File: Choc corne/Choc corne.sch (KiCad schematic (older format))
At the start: 43 parts, among them U1 ProMicro

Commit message: Started pcb
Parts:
- added J1: MJ-4PP-9, symbol kbd:MJ-4PP-9
- added OL1: OLED, symbol kbd:OLED
- added SW1: SW_PUSH, symbol kbd:SW_PUSH
- MX1, MX10, MX11, MX12, MX13, MX14, MX15, MX16, MX17, MX18, MX19, MX2, MX20, MX3, MX4, MX5, MX6, MX7, MX8, MX9: footprint Keebio-Parts:MX-Alps-Choc-1U-NoLED -> Keebio-Parts:Kailh-PG1350-1u-NoLED
- MX21: footprint Keebio-Parts:MX-Alps-Choc-1U-NoLED -> Keebio-Parts:Kailh-PG1350-1.5u
- U1: value ProMicro -> Elite-C; footprint Keebio-Parts:Elite-C-ZigZag -> Keebio-Parts:Elite-C
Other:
- moved on the sheet: U1
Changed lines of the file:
@@
 L promicro:ProMicro U1
 U 1 1 64503A13
-P 6050 3750
-F 0 "U1" H 6050 4787 60  0000 C CNN
-F 1 "ProMicro" H 6050 4681 60  0000 C CNN
-F 2 "Keebio-Parts:Elite-C-ZigZag" H 6150 2700 60  0001 C CNN
-F 3 "" H 6150 2700 60  0000 C CNN
-	1    6050 3750
+P 6100 3050
+F 0 "U1" H 6100 4087 60  0000 C CNN
+F 1 "Elite-C" H 6100 3981 60  0000 C CNN
+F 2 "Keebio-Parts:Elite-C" H 6200 2000 60  0001 C CNN
+F 3 "" H 6200 2000 60  0000 C CNN
+	1    6100 3050
 	1    0    0    -1
 $EndComp
@@
 F 0 "MX1" H 1583 2823 60  0000 C CNN
 F 1 "MX-NoLED" H 1583 2749 20  0000 C CNN
-F 2 "Keebio-Parts:MX-Alps-Choc-1U-NoLED" H 925 2575 60  0001 C CNN
+F 2 "Keebio-Parts:Kailh-PG1350-1u-NoLED" H 925 2575 60  0001 C CNN
 F 3 "" H 925 2575 60  0001 C CNN
 	1    1550 2600
@@
 F 0 "MX2" H 2183 2823 60  0000 C CNN
 F 1 "MX-NoLED" H 2183 2749 20  0000 C CNN
-F 2 "Keebio-Parts:MX-Alps-Choc-1U-NoLED" H 1525 2575 60  0001 C CNN
+F 2 "Keebio-Parts:Kailh-PG1350-1u-NoLED" H 1525 2575 60  0001 C CNN
 F 3 "" H 1525 2575 60  0001 C CNN
 	1    2150 2600
@@
 F 0 "MX3" H 2783 2823 60  0000 C CNN
 F 1 "MX-NoLED" H 2783 2749 20  0000 C CNN
-F 2 "Keebio-Parts:MX-Alps-Choc-1U-NoLED" H 2125 2575 60  0001 C CNN
+F 2 "Keebio-Parts:Kailh-PG1350-1u-NoLED" H 2125 2575 60  0001 C CNN
 F 3 "" H 2125 2575 60  0001 C CNN
 	1    2750 2600
@@
 F 0 "MX4" H 3383 2823 60  0000 C CNN
 F 1 "MX-NoLED" H 3383 2749 20  0000 C CNN
-F 2 "Keebio-Parts:MX-Alps-Choc-1U-NoLED" H 2725 2575 60  0001 C CNN
+F 2 "Keebio-Parts:Kailh-PG1350-1u-NoLED" H 2725 2575 60  0001 C CNN
 F 3 "" H 2725 2575 60  0001 C CNN
 	1    3350 2600
@@
 F 0 "MX5" H 3983 2823 60  0000 C CNN
 F 1 "MX-NoLED" H 3983 2749 20  0000 C CNN
-F 2 "Keebio-Parts:MX-Alps-Choc-1U-NoLED" H 3325 2575 60  0001 C CNN
+F 2 "Keebio-Parts:Kailh-PG1350-1u-NoLED" H 3325 2575 60  0001 C CNN
 F 3 "" H 3325 2575 60  0001 C CNN
 	1    3950 2600
@@
 F 0 "MX6" H 4583 2823 60  0000 C CNN
 F 1 "MX-NoLED" H 4583 2749 20  0000 C CNN
-F 2 "Keebio-Parts:MX-Alps-Choc-1U-NoLED" H 3925 2575 60  0001 C CNN
+F 2 "Keebio-Parts:Kailh-PG1350-1u-NoLED" H 3925 2575 60  0001 C CNN
 F 3 "" H 3925 2575 60  0001 C CNN
 	1    4550 2600
@@
 F 0 "MX7" H 1583 3573 60  0000 C CNN
 F 1 "MX-NoLED" H 1583 3499 20  0000 C CNN
-F 2 "Keebio-Parts:MX-Alps-Choc-1U-NoLED" H 925 3325 60  0001 C CNN
+F 2 "Keebio-Parts:Kailh-PG1350-1u-NoLED" H 925 3325 60  0001 C CNN
 F 3 "" H 925 3325 60  0001 C CNN
 	1    1550 3350
@@
 F 0 "MX8" H 2183 3573 60  0000 C CNN
 F 1 "MX-NoLED" H 2183 3499 20  0000 C CNN
-F 2 "Keebio-Parts:MX-Alps-Choc-1U-NoLED" H 1525 3325 60  0001 C CNN
+F 2 "Keebio-Parts:Kailh-PG1350-1u-NoLED" H 1525 3325 60  0001 C CNN
 F 3 "" H 1525 3325 60  0001 C CNN
 	1    2150 3350
@@
 F 0 "MX9" H 2783 3573 60  0000 C CNN
 F 1 "MX-NoLED" H 2783 3499 20  0000 C CNN
-F 2 "Keebio-Parts:MX-Alps-Choc-1U-NoLED" H 2125 3325 60  0001 C CNN
+F 2 "Keebio-Parts:Kailh-PG1350-1u-NoLED" H 2125 3325 60  0001 C CNN
 F 3 "" H 2125 3325 60  0001 C CNN
 	1    2750 3350
@@
 F 0 "MX10" H 3383 3573 60  0000 C CNN
 F 1 "MX-NoLED" H 3383 3499 20  0000 C CNN
-F 2 "Keebio-Parts:MX-Alps-Choc-1U-NoLED" H 2725 3325 60  0001 C CNN
+F 2 "Keebio-Parts:Kailh-PG1350-1u-NoLED" H 2725 3325 60  0001 C CNN
 F 3 "" H 2725 3325 60  0001 C CNN
 	1    3350 3350
@@
 F 0 "MX11" H 3983 3573 60  0000 C CNN
 F 1 "MX-NoLED" H 3983 3499 20  0000 C CNN
-F 2 "Keebio-Parts:MX-Alps-Choc-1U-NoLED" H 3325 3325 60  0001 C CNN
+F 2 "Keebio-Parts:Kailh-PG1350-1u-NoLED" H 3325 3325 60  0001 C CNN
 F 3 "" H 3325 3325 60  0001 C CNN
 	1    3950 3350
@@
 F 0 "MX12" H 4583 3573 60  0000 C CNN
 F 1 "MX-NoLED" H 4583 3499 20  0000 C CNN
-F 2 "Keebio-Parts:MX-Alps-Choc-1U-NoLED" H 3925 3325 60  0001 C CNN
+F 2 "Keebio-Parts:Kailh-PG1350-1u-NoLED" H 3925 3325 60  0001 C CNN
 F 3 "" H 3925 3325 60  0001 C CNN
 	1    4550 3350
@@
 F 0 "MX13" H 1583 4323 60  0000 C CNN
 F 1 "MX-NoLED" H 1583 4249 20  0000 C CNN
-F 2 "Keebio-Parts:MX-Alps-Choc-1U-NoLED" H 925 4075 60  0001 C CNN
+F 2 "Keebio-Parts:Kailh-PG1350-1u-NoLED" H 925 4075 60  0001 C CNN
 F 3 "" H 925 4075 60  0001 C CNN
 	1    1550 4100
@@
 F 0 "MX14" H 2183 4323 60  0000 C CNN
 F 1 "MX-NoLED" H 2183 4249 20  0000 C CNN
-F 2 "Keebio-Parts:MX-Alps-Choc-1U-NoLED" H 1525 4075 60  0001 C CNN
+F 2 "Keebio-Parts:Kailh-PG1350-1u-NoLED" H 1525 4075 60  0001 C CNN
 F 3 "" H 1525 4075 60  0001 C CNN
 	1    2150 4100
@@
 F 0 "MX15" H 2783 4323 60  0000 C CNN
 F 1 "MX-NoLED" H 2783 4249 20  0000 C CNN
-F 2 "Keebio-Parts:MX-Alps-Choc-1U-NoLED" H 2125 4075 60  0001 C CNN
+F 2 "Keebio-Parts:Kailh-PG1350-1u-NoLED" H 2125 4075 60  0001 C CNN
 F 3 "" H 2125 4075 60  0001 C CNN
 	1    2750 4100
@@
 F 0 "MX16" H 3383 4323 60  0000 C CNN
 F 1 "MX-NoLED" H 3383 4249 20  0000 C CNN
-F 2 "Keebio-Parts:MX-Alps-Choc-1U-NoLED" H 2725 4075 60  0001 C CNN
+F 2 "Keebio-Parts:Kailh-PG1350-1u-NoLED" H 2725 4075 60  0001 C CNN
 F 3 "" H 2725 4075 60  0001 C CNN
 	1    3350 4100
@@
 F 0 "MX17" H 3983 4323 60  0000 C CNN
 F 1 "MX-NoLED" H 3983 4249 20  0000 C CNN
-F 2 "Keebio-Parts:MX-Alps-Choc-1U-NoLED" H 3325 4075 60  0001 C CNN
+F 2 "Keebio-Parts:Kailh-PG1350-1u-NoLED" H 3325 4075 60  0001 C CNN
 F 3 "" H 3325 4075 60  0001 C CNN
 	1    3950 4100
@@
 F 0 "MX18" H 4583 4323 60  0000 C CNN
 F 1 "MX-NoLED" H 4583 4249 20  0000 C CNN
-F 2 "Keebio-Parts:MX-Alps-Choc-1U-NoLED" H 3925 4075 60  0001 C CNN
+F 2 "Keebio-Parts:Kailh-PG1350-1u-NoLED" H 3925 4075 60  0001 C CNN
 F 3 "" H 3925 4075 60  0001 C CNN
 	1    4550 4100
@@
 F 0 "MX19" H 3383 5073 60  0000 C CNN
 F 1 "MX-NoLED" H 3383 4999 20  0000 C CNN
-F 2 "Keebio-Parts:MX-Alps-Choc-1U-NoLED" H 2725 4825 60  0001 C CNN
+F 2 "Keebio-Parts:Kailh-PG1350-1u-NoLED" H 2725 4825 60  0001 C CNN
 F 3 "" H 2725 4825 60  0001 C CNN
 	1    3350 4850
@@
 F 0 "MX20" H 3983 5073 60  0000 C CNN
 F 1 "MX-NoLED" H 3983 4999 20  0000 C CNN
-F 2 "Keebio-Parts:MX-Alps-Choc-1U-NoLED" H 3325 4825 60  0001 C CNN
+F 2 "Keebio-Parts:Kailh-PG1350-1u-NoLED" H 3325 4825 60  0001 C CNN
 F 3 "" H 3325 4825 60  0001 C CNN
 	1    3950 4850
@@
 F 0 "MX21" H 4583 5073 60  0000 C CNN
 F 1 "MX-NoLED" H 4583 4999 20  0000 C CNN
-F 2 "Keebio-Parts:MX-Alps-Choc-1U-NoLED" H 3925 4825 60  0001 C CNN
+F 2 "Keebio-Parts:Kailh-PG1350-1.5u" H 3925 4825 60  0001 C CNN
 F 3 "" H 3925 4825 60  0001 C CNN
 	1    4550 4850
@@
 Text GLabel 2800 5300 0    50   Input ~ 0
 ROW3
+$Comp
+L kbd:MJ-4PP-9 J1
+U 1 1 64591E95
+P 6000 5650
+F 0 "J1" H 5820 5608 50  0000 R CNN
+F 1 "MJ-4PP-9" H 5820 5699 50  0000 R CNN
+F 2 "" H 6275 5825 50  0001 C CNN
+F 3 "~" H 6275 5825 50  0001 C CNN
+	1    6000 5650
+	-1   0    0    1
+$EndComp
+$Comp
+L kbd:OLED OL1
+U 1 1 645939B3
+P 6050 4150
+F 0 "OL1" V 6011 3822 51  0000 R CNN
+F 1 "OLED" V 5921 3822 47  0000 R CNN
+F 2 "" H 6050 4250 60  0001 C CNN
+F 3 "" H 6050 4250 60  0001 C CNN
+	1    6050 4150
+	0    -1   -1   0
+$EndComp
+$Comp
+L kbd:SW_PUSH SW1
+U 1 1 64598CCE
+P 6050 5300
+F 0 "SW1" H 6050 5555 50  0000 C CNN
+F 1 "SW_PUSH" H 6050 5464 50  0000 C CNN
+F 2 "" H 6050 5300 50  0000 C CNN
+F 3 "" H 6050 5300 50  0000 C CNN
+	1    6050 5300
+	1    0    0    -1
+$EndComp
 $EndSCHEMATC

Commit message: big update
whatever
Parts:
- added D22, D23, D24, D25, D26, D27, D28, D29, D30, D31, D32, D33, D34, D35, D36, D37, D38, D39, D40, D41, D42: CD4148W, Diode_SMD:D_0805_2012Metric, symbol Diode:CD4148W
- added J2: MJ-4PP-9, Keebio-Parts:TRRS-PJ-320A, symbol kbd:MJ-4PP-9
- added MX22, MX23, MX24, MX25, MX26, MX27, MX28, MX29, MX30, MX31, MX32, MX33, MX34, MX35, MX36, MX37, MX38, MX39, MX41, MX42: MX-NoLED, kbd:CherryMX_ChocV2_1u, symbol MX_Alps_Hybrid:MX-NoLED
- added MX40: MX-NoLED, kbd:CherryMX_ChocV2_1.5u, symbol MX_Alps_Hybrid:MX-NoLED
- added OL2: OLED, kbd:OLED_1side, symbol kbd:OLED
- added SW2: SW_PUSH, kbd:ResetSW_1side, symbol kbd:SW_PUSH
- added U2: Elite-C, Keebio-Parts:Elite-C, symbol promicro:ProMicro
- J1: footprint (none) -> Keebio-Parts:TRRS-PJ-320A
- MX1, MX10, MX11, MX12, MX13, MX14, MX15, MX16, MX17, MX18, MX19, MX2, MX20, MX3, MX4, MX5, MX6, MX7, MX8, MX9: footprint Keebio-Parts:Kailh-PG1350-1u-NoLED -> kbd:CherryMX_ChocV2_1u
- MX21: footprint Keebio-Parts:Kailh-PG1350-1.5u -> kbd:CherryMX_ChocV2_1.5u
- OL1: footprint (none) -> kbd:OLED_1side
- SW1: footprint (none) -> kbd:ResetSW_1side
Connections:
- net DATA: now reaches U1.2 (RX)
- net DATA: now also J1.B
- net VCC: now reaches U1.21 (VCC)
- net VCC: now also J1.D, OL1.3 (VCC)
- net RESET: now reaches U1.22 (RST)
- net RESET: now also SW1.1
- net GND: now reaches U1.23 (GND)
- net GND: now also J1.C, OL1.4 (GND), SW1.2, U1.3 (GND), U1.4 (GND)
- net SDA: now reaches U1.5 (SDA)
- net SDA: now also OL1.1 (SDA)
- net SCL: now reaches U1.6 (SCL)
- net SCL: now also OL1.2 (SCL)
- new net: D22.2 (A), MX22.2 (ROW)
- new net: D23.2 (A), MX23.2 (ROW)
- new net: D24.2 (A), MX24.2 (ROW)
- new net: D25.2 (A), MX25.2 (ROW)
- new net: D26.2 (A), MX26.2 (ROW)
- new net: D27.2 (A), MX27.2 (ROW)
- new net: D28.2 (A), MX28.2 (ROW)
- new net: D29.2 (A), MX29.2 (ROW)
- new net: D30.2 (A), MX30.2 (ROW)
- new net: D31.2 (A), MX31.2 (ROW)
- new net: D32.2 (A), MX32.2 (ROW)
- new net: D33.2 (A), MX33.2 (ROW)
- new net: D34.2 (A), MX34.2 (ROW)
- new net: D35.2 (A), MX35.2 (ROW)
- new net: D36.2 (A), MX36.2 (ROW)
- new net: D37.2 (A), MX37.2 (ROW)
- new net: D38.2 (A), MX38.2 (ROW)
- new net: D39.2 (A), MX39.2 (ROW)
- new net: D40.2 (A), MX40.2 (ROW)
- new net: D41.2 (A), MX41.2 (ROW)
- new net: D42.2 (A), MX42.2 (ROW)
- new net COL10: MX26.1 (COL), MX32.1 (COL), MX38.1 (COL)
- new net COL11: MX27.1 (COL), MX33.1 (COL), MX39.1 (COL)
- new net COL6: MX22.1 (COL), MX28.1 (COL), MX34.1 (COL), MX40.1 (COL)
- new net COL7: MX23.1 (COL), MX29.1 (COL), MX35.1 (COL), MX41.1 (COL)
- new net COL8: MX24.1 (COL), MX30.1 (COL), MX36.1 (COL), MX42.1 (COL)
- new net COL9: MX25.1 (COL), MX31.1 (COL), MX37.1 (COL)
- new net DATA_R: J2.B, U2.2 (RX)
- new net GNDA: J2.C, OL2.4 (GND), SW2.2, U2.23 (GND), U2.3 (GND), U2.4 (GND)
- new net RESET_R: SW2.1, U2.22 (RST)
- new net ROW4: D22.1 (K), D23.1 (K), D24.1 (K), D25.1 (K), D26.1 (K), D27.1 (K)
- new net ROW5: D28.1 (K), D29.1 (K), D30.1 (K), D31.1 (K), D32.1 (K), D33.1 (K)
- new net ROW6: D34.1 (K), D35.1 (K), D36.1 (K), D37.1 (K), D38.1 (K), D39.1 (K)
- new net ROW8: D40.1 (K), D41.1 (K), D42.1 (K)
- new net SCL_R: OL2.2 (SCL), U2.5 (SDA), U2.6 (SCL)
- new net SDA_R: OL2.1 (SDA)
- new net VDD: J2.D, OL2.3 (VCC)
- no-connect marks 0 -> 4
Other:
- moved on the sheet: D1, D10, D11, D12, D13, D14, D15, D16, D17, D18, D19, D2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

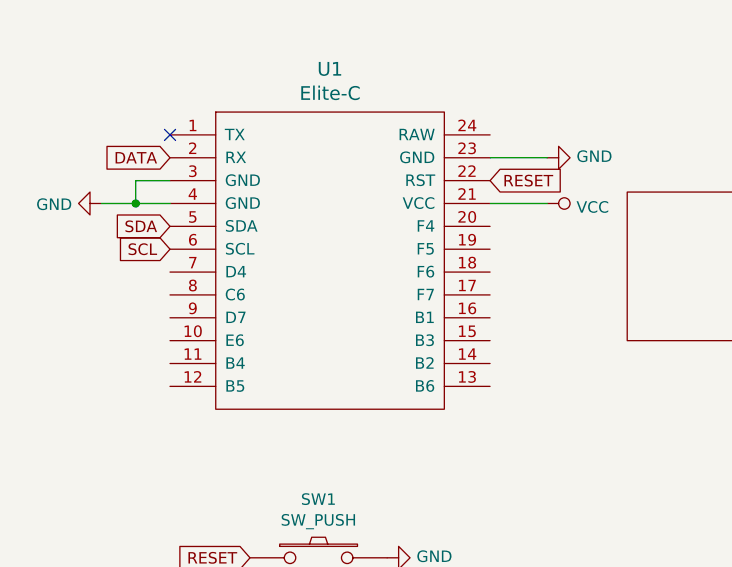
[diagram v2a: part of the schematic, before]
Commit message: Added partial pcb routing
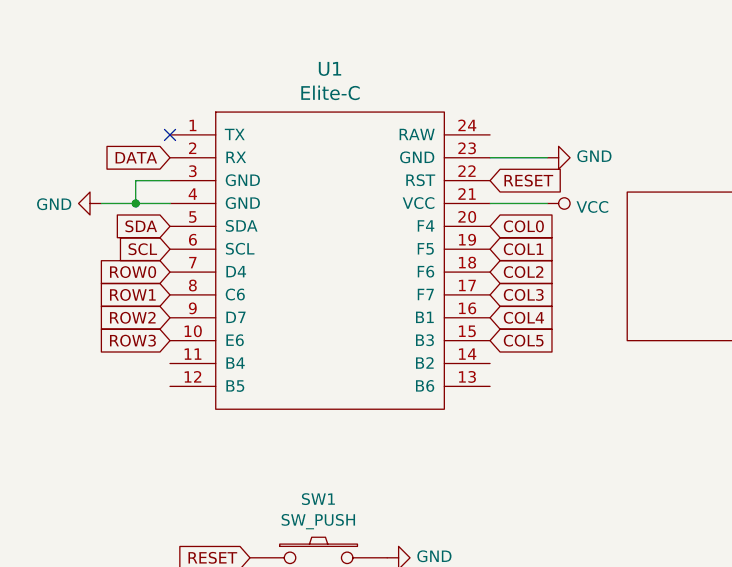
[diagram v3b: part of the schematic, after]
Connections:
- net COL0: now also U1.20 (F4)
- net COL1: now also U1.19 (F5)
- net COL2: now also U1.18 (F6)
- net COL3: now also U1.17 (F7)
- net COL4: now also U1.16 (B1)
- net COL5: now also U1.15 (B3)
- net ROW0: now also U1.7 (D4)
- net ROW1: now also U1.8 (C6)
- net ROW2: now also U1.9 (D7)
- net ROW3: now also U1.10 (E6)
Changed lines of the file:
@@
 Text GLabel 7150 4250 2    50   Input ~ 0
 ROW8
+Text GLabel 1200 5500 0    50   Input ~ 0
+ROW0
+Text GLabel 1200 5600 0    50   Input ~ 0
+ROW1
+Text GLabel 1200 5700 0    50   Input ~ 0
+ROW2
+Text GLabel 1200 5800 0    50   Input ~ 0
+ROW3
+Text GLabel 2600 5300 2    50   Input ~ 0
+COL0
+Text GLabel 2600 5400 2    50   Input ~ 0
+COL1
+Text GLabel 2600 5500 2    50   Input ~ 0
+COL2
+Text GLabel 2600 5600 2    50   Input ~ 0
+COL3
+Text GLabel 2600 5700 2    50   Input ~ 0
+COL4
+Text GLabel 2600 5800 2    50   Input ~ 0
+COL5
 $EndSCHEMATC
